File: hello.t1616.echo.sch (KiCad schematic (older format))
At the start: 4 parts, among them J1 Conn_01x03_Male, J2 Conn_FTDI_01x06_Male, U1 ATtiny1616-S

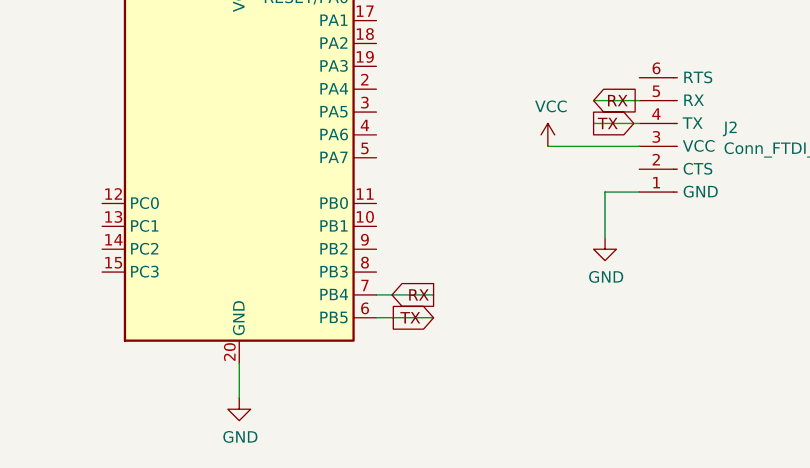
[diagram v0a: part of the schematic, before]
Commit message: Moved serial lines to correct pins.
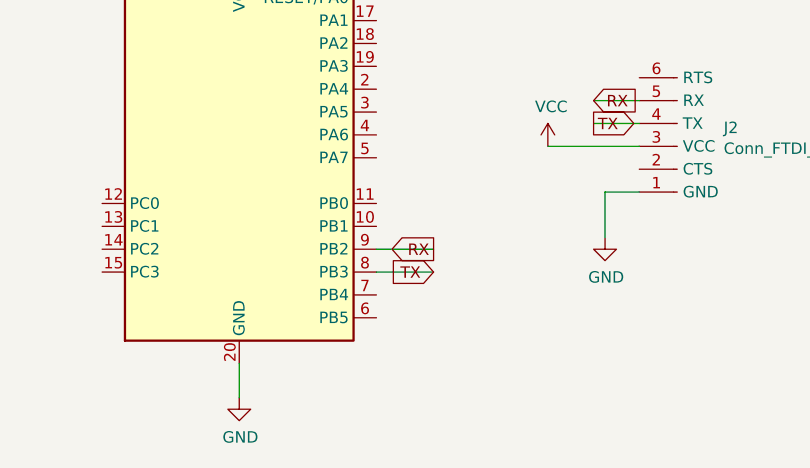
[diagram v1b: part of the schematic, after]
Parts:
- J1: footprint Connector_PinHeader_2.54mm:PinHeader_1x03_P2.54mm_Horizontal -> fab:Header_SMD_01x03_P2.54mm_Horizontal_Male
- J2: footprint Connector_PinHeader_2.54mm:PinHeader_1x06_P2.54mm_Vertical -> fab:Header_SMD_01x06_P2.54mm_Horizontal_Male
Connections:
- net RX: now also U1.9 (PB2); no longer U1.7 (PB4)
- net TX: now also U1.8 (PB3); no longer U1.6 (PB5)
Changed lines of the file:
@@
 F 0 "J2" H 7181 3519 50  0000 R CNN
 F 1 "Conn_FTDI_01x06_Male" H 7181 3610 50  0000 R CNN
-F 2 "Connector_PinHeader_2.54mm:PinHeader_1x06_P2.54mm_Vertical" H 7350 3600 50  0001 C CNN
+F 2 "fab:Header_SMD_01x06_P2.54mm_Horizontal_Male" H 7350 3600 50  0001 C CNN
 F 3 "~" H 7350 3600 50  0001 C CNN
 	1    7350 3600
@@
 F 0 "J1" H 5708 2431 50  0000 C CNN
 F 1 "Conn_01x03_Male" H 5708 2340 50  0000 C CNN
-F 2 "Connector_PinHeader_2.54mm:PinHeader_1x03_P2.54mm_Horizontal" H 5600 2150 50  0001 C CNN
+F 2 "fab:Header_SMD_01x03_P2.54mm_Horizontal_Male" H 5600 2150 50  0001 C CNN
 F 3 "~" H 5600 2150 50  0001 C CNN
 	1    5600 2150
@@
 $EndComp
 Wire Wire Line
-	6000 4350 6250 4350
+	6000 4150 6250 4150
 Wire Wire Line
-	6000 4250 6250 4250
-Text GLabel 6250 4350 0    50   Input ~ 0
+	6000 4050 6250 4050
+Text GLabel 6250 4150 0    50   Input ~ 0
 TX
-Text GLabel 6250 4250 0    50   Output ~ 0
+Text GLabel 6250 4050 0    50   Output ~ 0
 RX
 $EndSCHEMATC
